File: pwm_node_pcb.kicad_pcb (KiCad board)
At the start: 4 copper layers, 49 x 14.2 mm, 36 parts, among them J1 External Power, J2 CAN1, U1 LD1117S33CTR, U2 TJA1051T/3, U3 AP63203WU, U4 TXB0104QPWRQ1, U5 STM32L432KCU

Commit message: Add re-layout WIP changes
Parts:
- removed the C7 at (165.7, 99.5)
- removed the J2 at (158.0, 97.8)
- removed L1: 10u, Inductor_SMD:L_0402_1005Metric
- added R4: 76k8, Resistor_SMD:R_0603_1608Metric, F.Cu at (145.3, 103.2)
- added TP1: TestPoint, TestPoint:TestPoint_Pad_D1.5mm, F.Cu at (141.3, 99.0)
- C3: footprint Capacitor_SMD:C_0603_1608Metric -> Capacitor_SMD:C_0805_2012Metric
- C4: value 100n -> 22u; footprint Capacitor_SMD:C_0603_1608Metric -> Capacitor_SMD:C_0805_2012Metric
- C5: value 100p -> 16n
- C6: value 22p -> 4n7
- J1: value External Power -> CAN1; moved to F.Cu
- J2: renamed from J3; value ~ -> TC2050-IDC-NL; footprint tag_connect:tag_connect_tc2030-idc-nl -> tag_connect:tag_connect_tc2050-idc-nl; moved to B.Cu
- R1: value 120R -> 60R
- R2: value 158k -> 60R
- R3: value 30k1 -> 76k8
- U3: value AP63203WU -> TPSM82903; footprint Package_TO_SOT_SMD:TSOT-23-6 -> ti_buck:tpsm8290x
- moved FM4 37.5 mm to (174.8, 83.8)
- moved FM2 29.7 mm to (165.0, 91.0)
- moved FM1 26.3 mm to (165.0, 93.8)
- moved C4 23.7 mm to (140.9, 108.0), turned to 0 degrees
- moved R3 21.1 mm to (139.7, 103.2)
- moved U3 21.1 mm to (142.4, 104.8), turned to 180 degrees
- moved C11 20.9 mm to (161.0, 97.5), turned to 180 degrees
- moved FM6 20.3 mm to (162.5, 84.8)
- moved C3 19.4 mm to (145.7, 107.0), turned to -90 degrees
- moved C5 19.0 mm to (143.8, 101.2)
- moved JP1 16.8 mm to (157.0, 98.5), turned to 90 degrees
- moved FM3 16.5 mm to (168.0, 91.0)
- moved FM5 14.2 mm to (158.5, 85.8)
- moved C10 12.9 mm to (165.9, 104.3), turned to 90 degrees
- moved JP2 9.40 mm to (153.0, 98.5)
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- renumbered C11 to C10, C12 to C11, C8 to C7, C9 to C8, C10 to C9, J4 to J3, R4 to R5, U5 to U4, U4 to U5
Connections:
- C3 pad 1: +V_{L} -> +VSUPPLY
- C4 pad 1: Net-(U3-SW) -> +5V
- C4 pad 2: Net-(U3-BST) -> GND
- C5 pad 1: +5V -> Net-(U3-SS/TR)
- C5 pad 2: Net-(U3-FB) -> GND
- C6 pad 1: +5V -> Net-(C6-Pad1)
- C6 pad 2: Net-(C6-Pad2) -> GND
- J1 pad 1: +V_{L} -> /CAN1+
- J1 pad 2: GND -> /CAN1-
- J2 pad 3: /NRST -> GND
- J3 pad 11: +V_{L} -> +5V
- J3 pad 2: +V_{L} -> +5V
- J3 pad 5: +V_{L} -> +5V
- J3 pad 8: +V_{L} -> +5V
- R1 pad 1: /CAN1+ -> /CAN1-
- R1 pad 2: /CAN1- -> Net-(C6-Pad1)
- R2 pad 1: +5V -> /CAN1+
- R2 pad 2: Net-(U3-FB) -> Net-(C6-Pad1)
- R3 pad 1: Net-(U3-FB) -> Net-(U3-FB/VSET)
- U3 pad 1: Net-(U3-FB) -> +VSUPPLY
- U3 pad 2: +V_{L} -> +VSUPPLY
- U3 pad 3: +V_{L} -> +VSUPPLY
- U3 pad 4: GND -> Net-(U3-MODE/S-CONF)
- U3 pad 5: Net-(U3-SW) -> Net-(U3-SS/TR)
- U3 pad 6: Net-(U3-BST) -> Net-(U3-PG)
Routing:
- net +V_{L}: track 26.7 -> 0.00 mm, vias 7 -> 0
- net +3V3: track 24.1 -> 15.7 mm, vias 6 -> 4
- net /PWM1_{5V}: track 7.15 -> 0.00 mm
- net /PWM2_{5V}: track 5.35 -> 0.00 mm
- net /CAN1-: track 8.80 -> 13.8 mm
- net Net-(U3-FB): track 4.72 -> 0.00 mm
- net Net-(U3-PG): track 0.00 -> 4.59 mm
- net +5V: track 8.93 -> 13.4 mm, vias 5 -> 6
- net /SWO: track 3.84 -> 8.15 mm, vias 0 -> 1
- net Net-(U3-SW): track 4.28 -> 0.00 mm
- net /PWM3_{5V}: track 4.16 -> 0.00 mm
- net /PWM4_{5V}: track 3.74 -> 0.00 mm
- net Net-(C6-Pad1): track 0.00 -> 3.02 mm
- net GND: track 26.2 -> 23.2 mm, vias 28 -> 44
- net /BOOT0: track 5.84 -> 3.42 mm
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- added copper zone on F.Cu, net +3V3
- added copper zone on F.Cu, net +5V
- added copper zone on B.Cu, net +VSUPPLY
- added copper zone on F.Cu, net +VSUPPLY
- removed copper zone on B.Cu, net +V_{L}
- removed copper zone on F.Cu, net +V_{L}
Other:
- board size 49 x 14.2 mm -> 48 x 14 mm
- board text removed: "B"
- board text removed: "G"
- board text removed: "H"
- board text removed: "L"
- board text removed: "R"
- board text removed: "S"
- board text removed: "V_{L}"

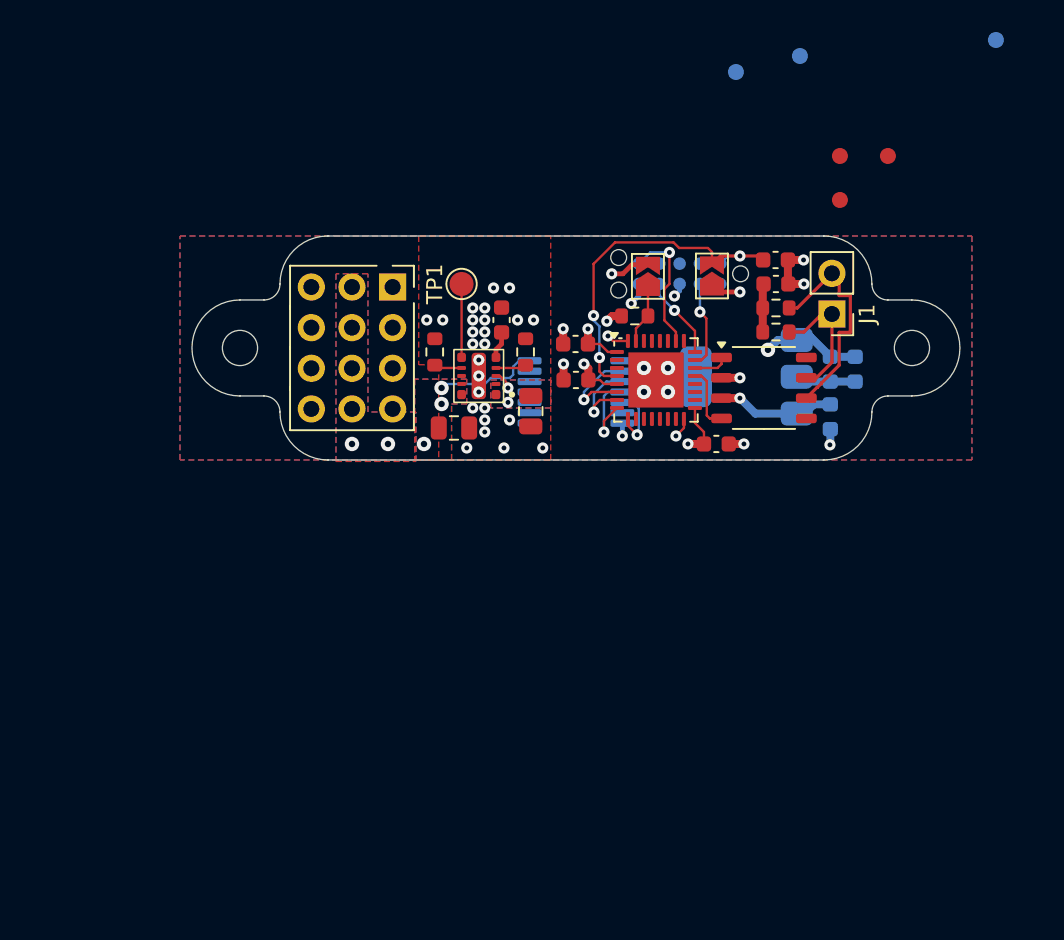
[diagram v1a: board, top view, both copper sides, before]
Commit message: Cleanup layout and routing
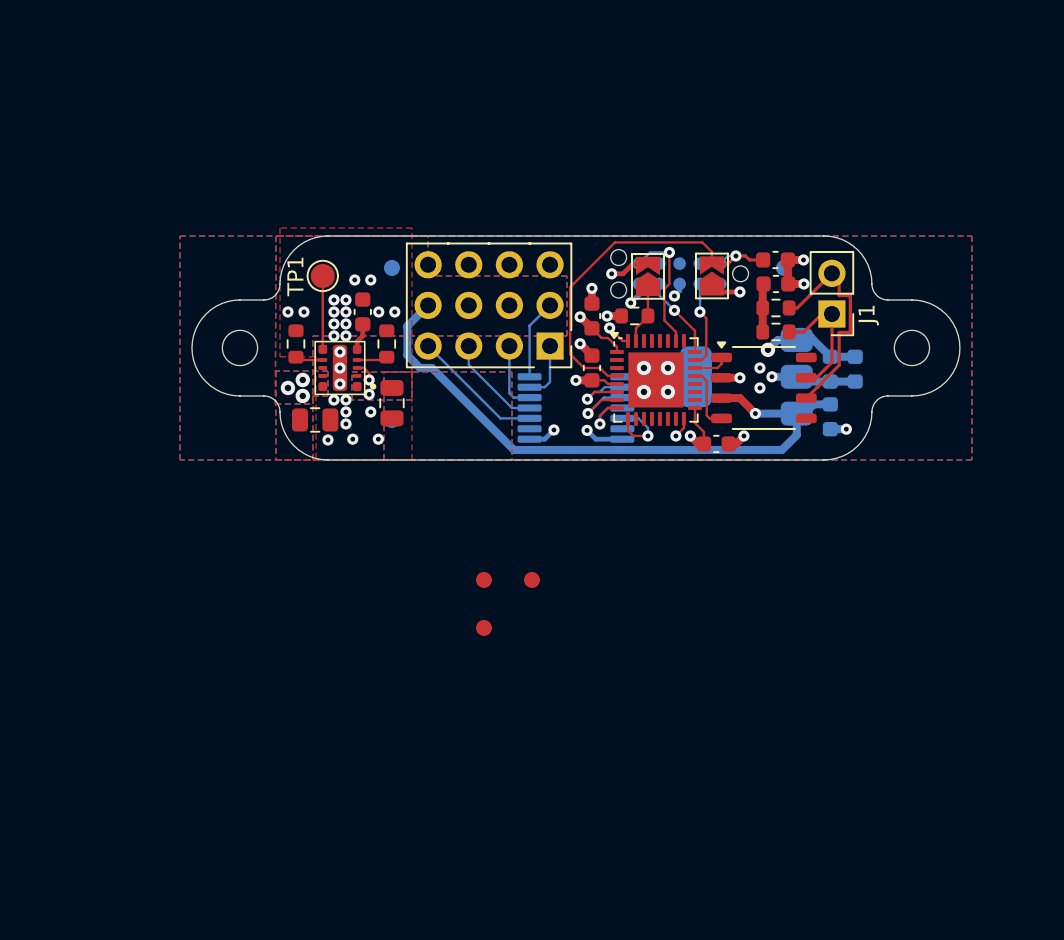
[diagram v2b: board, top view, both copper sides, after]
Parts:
- moved FM4 44.6 mm to (137.0, 107.5)
- moved FM1 34.8 mm to (142.8, 120.5)
- moved FM2 34.6 mm to (142.8, 117.5)
- moved FM3 34.6 mm to (145.8, 117.5)
- moved FM5 24.7 mm to (137.0, 98.0)
- moved FM6 13.3 mm to (161.5, 98.0)
- moved J3 8.97 mm to (143.1, 100.3), turned to 180 degrees
- moved C3 8.69 mm to (137.0, 106.5)
- moved C4 8.69 mm to (132.2, 107.5)
- moved R3 8.69 mm to (131.0, 102.8)
- moved U3 8.69 mm to (133.8, 104.2)
- moved C5 8.69 mm to (135.2, 100.8)
- moved R4 8.69 mm to (136.7, 102.8)
- moved TP1 8.69 mm to (132.7, 98.5)
- moved C7 2.03 mm to (149.5, 101.0), turned to 90 degrees
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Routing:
- net +5V: track 13.4 -> 44.0 mm, vias 6 -> 4
- net /PWM4_{5V}: track 0.00 -> 8.21 mm
- net /PWM3_{5V}: track 0.00 -> 6.09 mm
- net /PWM2_{5V}: track 0.00 -> 4.33 mm
- net +3V3: track 15.7 -> 20.0 mm, vias 4 -> 8
- net /PWM1_{5V}: track 0.00 -> 3.66 mm
- net GND: track 23.2 -> 25.0 mm
- net /TIM1_CH3: track 5.34 -> 3.88 mm
- net /NRST: track 22.0 -> 23.4 mm, vias 3 -> 1
- net /TIM1_CH1: track 5.68 -> 4.53 mm

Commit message: Revamp schematic and nuke PCB
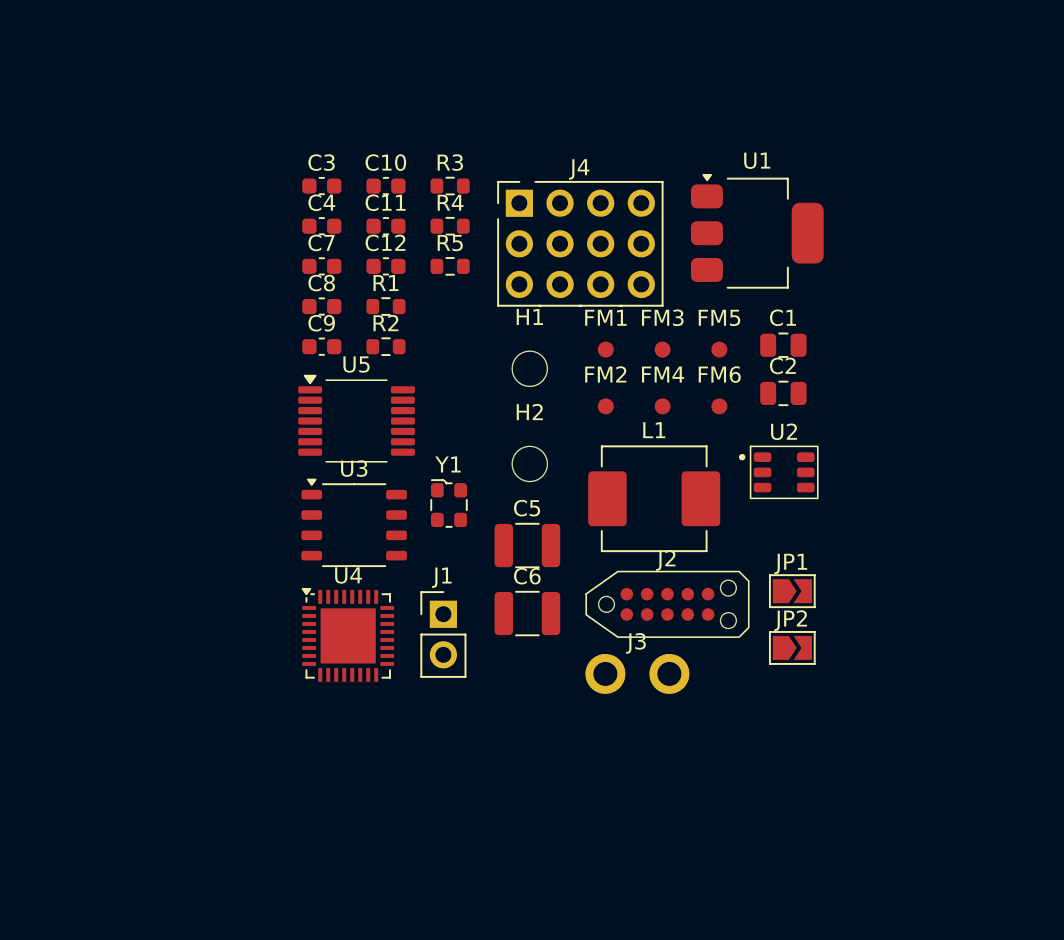
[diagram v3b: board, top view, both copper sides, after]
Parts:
- removed TP1: TestPoint, TestPoint:TestPoint_Pad_D1.5mm
- added C12: 100n, Capacitor_SMD:C_0603_1608Metric, F.Cu at (136.6, 97.9)
- added J4: ~, pwm_node_connectors:3x4_2-54mm_breakout, F.Cu at (148.8, 96.5)
- added L1: 6u8, pwm_node_inductor:vishay_ihlp-2525cz, F.Cu at (153.4, 112.4)
- added Y1: ECS-2520MV-080-BN, Oscillator:Oscillator_SMD_ECS_2520MV-xxx-xx-4Pin_2.5x2.0mm, F.Cu at (140.6, 112.8)
- C1: footprint Capacitor_SMD:C_0603_1608Metric -> Capacitor_SMD:C_0805_2012Metric; moved to F.Cu
- C10: value 4u7 -> 100n; moved to F.Cu
- C11: value 100n -> 4u7
- C2: value 10u -> 2u2; footprint Capacitor_SMD:C_0603_1608Metric -> Capacitor_SMD:C_0805_2012Metric; moved to F.Cu
- C3: value 10u -> 100n; footprint Capacitor_SMD:C_0805_2012Metric -> Capacitor_SMD:C_0603_1608Metric
- C4: value 22u -> 10u; footprint Capacitor_SMD:C_0805_2012Metric -> Capacitor_SMD:C_0603_1608Metric
- C5: value 16n -> 22u; footprint Capacitor_SMD:C_0603_1608Metric -> Capacitor_SMD:C_1210_3225Metric
- C6: value 4n7 -> 22u; footprint Capacitor_SMD:C_0603_1608Metric -> Capacitor_SMD:C_1210_3225Metric
- C7: value 100n -> 4n7
- FM4, FM5, FM6, J2, U1, U5: moved to F.Cu
- J3: value ~ -> Battery; footprint pwm_node_connector:3x4_2-54mm_breakout -> pwm_node_connectors:battery
- R1: value 60R -> 100k
- R2: value 60R -> 13k7
- R3, R4: value 76k8 -> 60R
- U2: value TJA1051T/3 -> LMR51430; footprint nxp:sot96-1_soic-8 -> ti_buck:lmr51430
- U3: value TPSM82903 -> TJA1051T/3; footprint ti_buck:tpsm8290x -> nxp:sot96-1_soic-8
- moved C10 31.5 mm to (136.6, 92.9), turned to 0 degrees
- moved J1 30.7 mm to (140.2, 119.6), turned to 0 degrees
- moved C6 25.8 mm to (145.5, 119.6)
- moved C9 25.4 mm to (132.6, 102.9)
- moved U4 25.0 mm to (134.3, 121.0)
- moved JP2 24.9 mm to (162.0, 121.8), turned to 0 degrees
- moved J3 24.8 mm to (152.3, 123.4), turned to 0 degrees
- moved C11 24.4 mm to (136.6, 95.4), turned to 0 degrees
- moved R2 24.4 mm to (136.6, 102.9), turned to 0 degrees
- moved R1 24.4 mm to (136.6, 100.4), turned to 0 degrees
- moved H1 23.9 mm to (145.6, 104.3)
- moved FM5 21.1 mm to (157.5, 103.1), turned to 0 degrees
- moved J2 20.7 mm to (154.2, 119.0), turned to 0 degrees
- moved JP1 20.3 mm to (162.0, 118.2), turned to 0 degrees
- moved H2 19.5 mm to (145.6, 110.2)
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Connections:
- C1 pad 1: +5V -> Net-(U2-CB)
- C1 pad 2: GND -> /BUCK_SW
- C11 pad 1: GND -> +3V3
- C11 pad 2: /NRST -> GND
- C2 pad 1: +3V3 -> +VSUPPLY
- C3 pad 1: +VSUPPLY -> +5V
- C4 pad 1: +5V -> +3V3
- C5 pad 1: Net-(U3-SS/TR) -> GND
- C5 pad 2: GND -> +5V
- C6 pad 1: Net-(C6-Pad1) -> GND
- C6 pad 2: GND -> +5V
- C7 pad 1: +3V3 -> Net-(C7-Pad1)
- J3 pad 1: /PWM1_{5V} -> +VSUPPLY
- J3 pad 2: +5V -> GND
- R1 pad 1: /CAN1- -> Net-(U2-FB)
- R1 pad 2: Net-(C6-Pad1) -> +5V
- R2 pad 1: /CAN1+ -> Net-(U2-FB)
- R2 pad 2: Net-(C6-Pad1) -> GND
- R3 pad 1: Net-(U3-FB/VSET) -> /CAN1-
- R3 pad 2: GND -> Net-(C7-Pad1)
- R4 pad 1: Net-(U3-MODE/S-CONF) -> /CAN1+
- R4 pad 2: GND -> Net-(C7-Pad1)
- U2 pad 1: /CAN1_TX -> GND
- U2 pad 2: GND -> /BUCK_SW
- U2 pad 3: +5V -> +VSUPPLY
- U2 pad 4: /CAN1_RX -> Net-(U2-FB)
- U2 pad 5: +3V3 -> +VSUPPLY
- U2 pad 6: /CAN1- -> Net-(U2-CB)
- U3 pad 1: +VSUPPLY -> /CAN1_TX
- U3 pad 2: +VSUPPLY -> GND
- U3 pad 3: +VSUPPLY -> +5V
- U3 pad 4: Net-(U3-MODE/S-CONF) -> /CAN1_RX
- U3 pad 5: Net-(U3-SS/TR) -> +3V3
- U3 pad 6: Net-(U3-PG) -> /CAN1-
- U3 pad 7: Net-(U3-FB/VSET) -> /CAN1+
- U4 pad 11: unconnected-(U4-PA5-Pad11) -> /TIM1_CH1
- U4 pad 6: /TIM1_CH1 -> Net-(U4-PA0)
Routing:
- net +5V: track 44.0 -> 0.00 mm, vias 4 -> 0
- net GND: track 25.0 -> 0.00 mm, vias 44 -> 0
- net /NRST: track 23.4 -> 0.00 mm, vias 1 -> 0
- net +3V3: track 20.0 -> 0.00 mm, vias 8 -> 0
- net /CAN1-: track 13.8 -> 0.00 mm
- net /PWM4_{5V}: track 8.21 -> 0.00 mm
- net /CAN1+: track 8.16 -> 0.00 mm
- net /SWO: track 8.15 -> 0.00 mm, vias 1 -> 0
- net /PWM3_{5V}: track 6.09 -> 0.00 mm
- net /SWDIO: track 5.45 -> 0.00 mm, vias 1 -> 0
- net /SWCLK: track 5.17 -> 0.00 mm, vias 1 -> 0
- net /TIM1_CH2: track 4.72 -> 0.00 mm, vias 1 -> 0
- net Net-(U3-PG): track 4.59 -> 0.00 mm
- net /TIM1_CH1: track 4.53 -> 0.00 mm, vias 1 -> 0
- net /TIM1_CH4: track 4.46 -> 0.00 mm, vias 1 -> 0
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- removed copper zone on B.Cu, net +3V3
- removed copper zone on F.Cu, net +3V3
- removed copper zone on B.Cu, net +5V
- removed copper zone on F.Cu, net +5V
- removed copper zone on B.Cu, net +VSUPPLY
- removed copper zone on F.Cu, net +VSUPPLY
- removed copper zone on F.Cu, net GND
- removed copper zone on In1.Cu, net GND
- removed copper zone on In2.Cu, net GND
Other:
- board outline removed
- board text removed: "30mm Radius"
- board text removed: "47.5mm Radius"

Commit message: Initial component placement
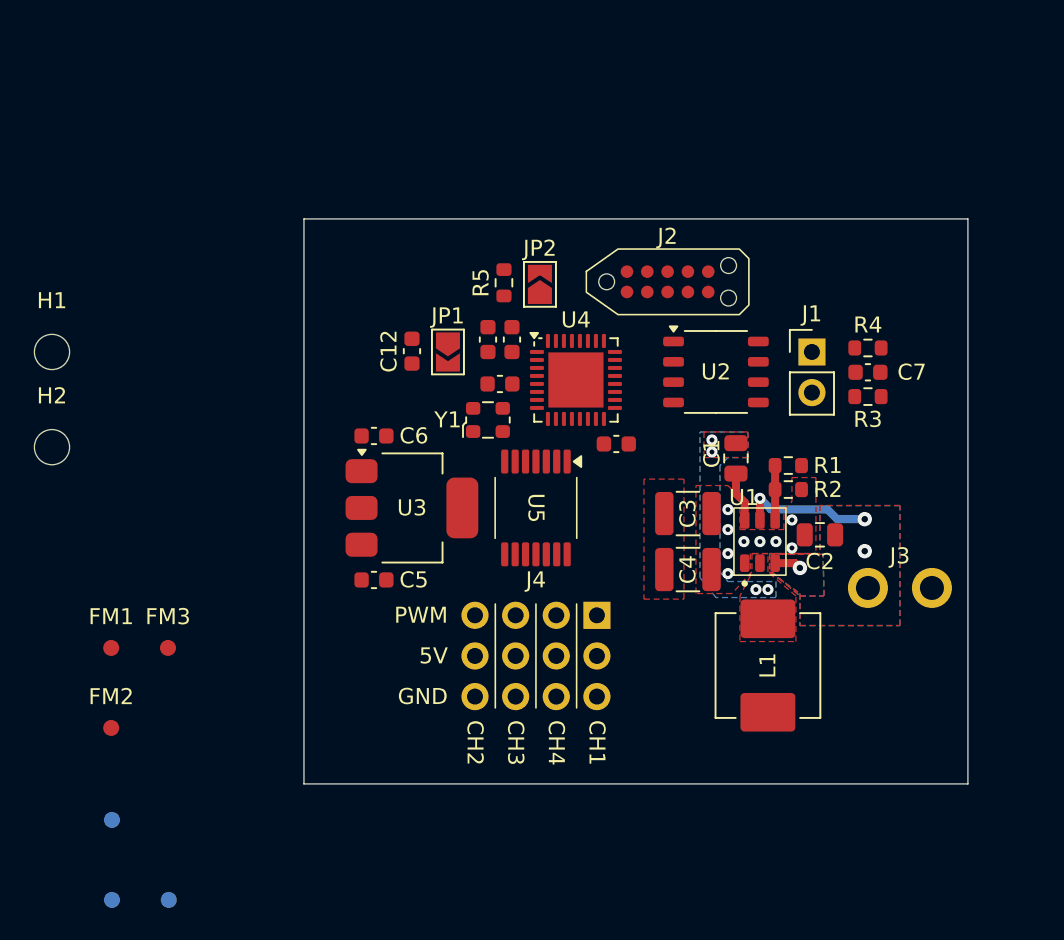
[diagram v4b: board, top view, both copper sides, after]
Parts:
- C3: value 100n -> 22u; footprint Capacitor_SMD:C_0603_1608Metric -> Capacitor_SMD:C_1210_3225Metric
- C4: value 10u -> 22u; footprint Capacitor_SMD:C_0603_1608Metric -> Capacitor_SMD:C_1210_3225Metric
- C5: value 22u -> 100n; footprint Capacitor_SMD:C_1210_3225Metric -> Capacitor_SMD:C_0603_1608Metric
- C6: value 22u -> 10u; footprint Capacitor_SMD:C_1210_3225Metric -> Capacitor_SMD:C_0603_1608Metric
- FM4, FM5, FM6, J4: moved to B.Cu
- U1: value LD1117S33CTR -> LMR51430; footprint Package_TO_SOT_SMD:SOT-223-3_TabPin2 -> ti_buck:lmr51430
- U2: value LMR51430 -> TJA1051T/3; footprint ti_buck:lmr51430 -> nxp:sot96-1_soic-8
- U3: value TJA1051T/3 -> LD1117S33CTR; footprint nxp:sot96-1_soic-8 -> Package_TO_SOT_SMD:SOT-223-3_TabPin2
- moved FM6 48.9 mm to (119.5, 137.5), turned to 180 degrees
- moved FM5 48.0 mm to (119.5, 132.5), turned to 180 degrees
- moved FM4 43.6 mm to (123.0, 137.5), turned to 180 degrees
- moved FM2 36.9 mm to (119.5, 126.8)
- moved FM1 36.1 mm to (119.5, 121.8)
- moved FM3 36.1 mm to (123.0, 121.8)
- moved C7 34.8 mm to (166.8, 104.5), turned to 180 degrees
- moved C4 31.4 mm to (155.5, 116.8), turned to 180 degrees
- moved C3 30.7 mm to (155.5, 113.3), turned to 180 degrees
- moved H1 29.9 mm to (115.8, 103.2)
- moved H2 29.9 mm to (115.8, 109.2)
- moved R3 29.2 mm to (166.8, 106.0)
- moved J1 28.3 mm to (163.2, 103.2)
- moved JP2 27.7 mm to (146.2, 99.0), turned to 90 degrees
- moved R4 27.2 mm to (166.8, 103.0)
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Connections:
- C1 pad 1: Net-(U2-CB) -> Net-(U1-CB)
- C3 pad 1: +5V -> GND
- C3 pad 2: GND -> +5V
- C4 pad 1: +3V3 -> GND
- C4 pad 2: GND -> +5V
- C5 pad 1: GND -> +5V
- C5 pad 2: +5V -> GND
- C6 pad 1: GND -> +3V3
- C6 pad 2: +5V -> GND
- J4 pad 10: /PWM4_{5V} -> /PWM2_{5V}
- J4 pad 4: /PWM2_{5V} -> /PWM4_{5V}
- R1 pad 1: Net-(U2-FB) -> Net-(U1-FB)
- R2 pad 1: Net-(U2-FB) -> Net-(U1-FB)
- U1 pad 2: +3V3 -> /BUCK_SW
- U1 pad 3: +5V -> +VSUPPLY
- U2 pad 1: GND -> /CAN1_TX
- U2 pad 2: /BUCK_SW -> GND
- U2 pad 3: +VSUPPLY -> +5V
- U2 pad 4: Net-(U2-FB) -> /CAN1_RX
- U2 pad 5: +VSUPPLY -> +3V3
- U2 pad 6: Net-(U2-CB) -> /CAN1-
- U3 pad 1: /CAN1_TX -> GND
- U3 pad 2: GND -> +3V3
- U5 pad 10: /PWM4_{5V} -> /PWM2_{5V}
- U5 pad 12: /PWM2_{5V} -> /PWM4_{5V}
- U5 pad 3: /TIM1_CH2 -> /TIM1_CH4
- U5 pad 5: /TIM1_CH4 -> /TIM1_CH2
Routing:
- net +VSUPPLY: track 0.00 -> 10.1 mm, vias 0 -> 4
- net Net-(U1-FB): track 0.00 -> 3.40 mm
- net Net-(U1-CB): track 0.00 -> 3.13 mm
- net GND: vias 0 -> 9
- net /BUCK_SW: vias 0 -> 4
- added copper zone on F.Cu, net +5V
- added copper zone on B.Cu, net +VSUPPLY
- added copper zone on F.Cu, net +VSUPPLY
- added copper zone on B.Cu, net /BUCK_SW
- added copper zone on F.Cu, net /BUCK_SW
- added copper zone on F.Cu, net GND
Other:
- board outline added: 41.5 x 35.3 mm
- board text added: "5V"
- board text added: "CH1"
- board text added: "CH2"
- board text added: "CH3"
- board text added: "CH4"
- board text added: "GND"
- board text added: "J4"
- board text added: "PWM"
